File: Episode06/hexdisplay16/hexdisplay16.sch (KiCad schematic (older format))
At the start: 24 parts, among them J1 Conn_02x05_Counter_Clockwise, J2 Conn_02x05_Counter_Clockwise, J3 Conn_02x05_Counter_Clockwise, J4 Conn_02x05_Counter_Clockwise, J5 Conn_01x02, J6 Conn_01x16, J7 Conn_01x06, Q1 MMBT3906, Q2 MMBT3906, Q3 MMBT3906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

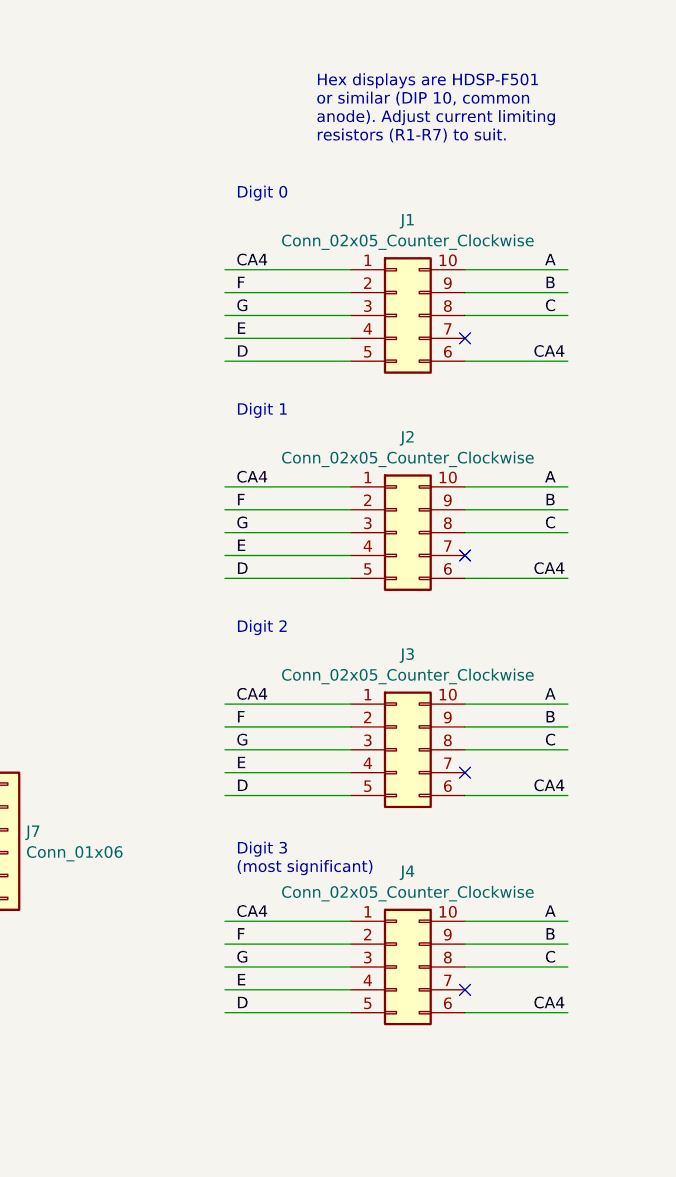
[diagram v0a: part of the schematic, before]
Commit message: fix common anode lines
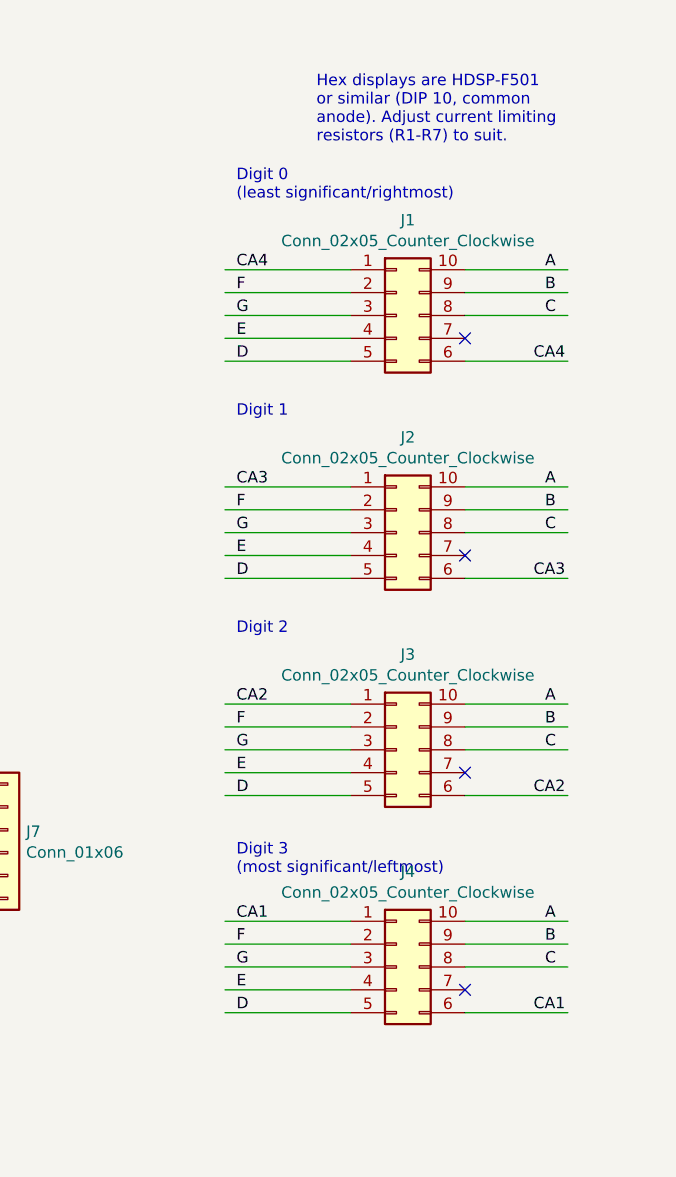
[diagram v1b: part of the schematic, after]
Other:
- note added: "Digit 0\n(least significant/rightmost)"
- note added: "Digit 3\n(most significant/leftmost)"
- note removed: "Digit 0"
- note removed: "Digit 3\n(most significant)"
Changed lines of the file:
@@
 Digit 1
 Text Notes 8500 2750 0    50   ~ 0
-Digit 0
+Digit 0\n(least significant/rightmost)
 Wire Wire Line
 	9000 3050 8450 3050
@@
 $EndComp
 Text Notes 8500 5700 0    50   ~ 0
-Digit 3\n(most significant)
+Digit 3\n(most significant/leftmost)
 Wire Wire Line
 	9000 3350 8450 3350
@@
 	9000 4000 8450 4000
 Text Label 8500 4000 0    50   ~ 0
-CA4
+CA3
 Wire Wire Line
 	9000 4400 8450 4400
@@
 	9000 4950 8450 4950
 Text Label 8500 4950 0    50   ~ 0
-CA4
+CA2
 Wire Wire Line
 	9000 5350 8450 5350
@@
 	9000 5900 8450 5900
 Text Label 8500 5900 0    50   ~ 0
-CA4
+CA1
 Wire Wire Line
 	9000 6300 8450 6300
@@
 	9500 4400 9950 4400
 Text Label 9800 4400 0    50   ~ 0
-CA4
+CA3
 Wire Wire Line
 	9500 4000 9950 4000
@@
 	9500 5350 9950 5350
 Text Label 9800 5350 0    50   ~ 0
-CA4
+CA2
 Wire Wire Line
 	9500 4950 9950 4950
@@
 	9500 6300 9950 6300
 Text Label 9800 6300 0    50   ~ 0
-CA4
+CA1
 Wire Wire Line
 	9500 5900 9950 5900

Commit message: assign packages
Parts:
- C1: footprint (none) -> Capacitor_SMD:C_1206_3216Metric_Pad1.33x1.80mm_HandSolder
- J1, J2, J3, J4: footprint (none) -> Package_DIP:DIP-10_W7.62mm
- J5: footprint (none) -> Connector_PinHeader_2.54mm:PinHeader_1x02_P2.54mm_Vertical
- J6: footprint (none) -> Connector_PinHeader_2.54mm:PinHeader_1x16_P2.54mm_Vertical
- J7: footprint (none) -> Connector_PinHeader_2.54mm:PinHeader_1x06_P2.54mm_Vertical
- Q1, Q2, Q3, Q4: footprint SOT95P240X120-3N -> Package_TO_SOT_SMD:SOT-23
- R1, R10, R11, R2, R3, R4, R5, R6, R7, R8, R9: footprint (none) -> Resistor_SMD:R_0805_2012Metric_Pad1.20x1.40mm_HandSolder
- U1: footprint QFP80P1200X1200X120-44N -> Package_QFP:LQFP-44_10x10mm_P0.8mm
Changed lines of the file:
@@
 F 0 "U1" H 4450 4170 50  0000 C CNN
 F 1 "ATMEGA164A-AU" H 4450 4079 50  0000 C CNN
-F 2 "QFP80P1200X1200X120-44N" H 4450 2400 50  0001 L BNN
+F 2 "Package_QFP:LQFP-44_10x10mm_P0.8mm" H 4450 2400 50  0001 L BNN
 F 3 "" H 4450 2400 50  0001 L BNN
 F 4 "1841601" H 4450 2400 50  0001 L BNN "OC_FARNELL"
@@
 F 0 "R1" V 1100 1650 50  0000 C CNN
 F 1 "330" V 1150 1900 50  0000 C CNN
-F 2 "" V 1080 1900 50  0001 C CNN
+F 2 "Resistor_SMD:R_0805_2012Metric_Pad1.20x1.40mm_HandSolder" V 1080 1900 50  0001 C CNN
 F 3 "" H 1150 1900 50  0001 C CNN
 	1    1150 1900
@@
 F 0 "R2" V 1100 1750 50  0000 C CNN
 F 1 "330" V 1150 2000 50  0000 C CNN
-F 2 "" V 1080 2000 50  0001 C CNN
+F 2 "Resistor_SMD:R_0805_2012Metric_Pad1.20x1.40mm_HandSolder" V 1080 2000 50  0001 C CNN
 F 3 "" H 1150 2000 50  0001 C CNN
 	1    1150 2000
@@
 F 0 "R3" V 1100 1850 50  0000 C CNN
 F 1 "330" V 1150 2100 50  0000 C CNN
-F 2 "" V 1080 2100 50  0001 C CNN
+F 2 "Resistor_SMD:R_0805_2012Metric_Pad1.20x1.40mm_HandSolder" V 1080 2100 50  0001 C CNN
 F 3 "" H 1150 2100 50  0001 C CNN
 	1    1150 2100
@@
 F 0 "R4" V 1100 1950 50  0000 C CNN
 F 1 "330" V 1150 2200 50  0000 C CNN
-F 2 "" V 1080 2200 50  0001 C CNN
+F 2 "Resistor_SMD:R_0805_2012Metric_Pad1.20x1.40mm_HandSolder" V 1080 2200 50  0001 C CNN
 F 3 "" H 1150 2200 50  0001 C CNN
 	1    1150 2200
@@
 F 0 "R5" V 1100 2050 50  0000 C CNN
 F 1 "330" V 1150 2300 50  0000 C CNN
-F 2 "" V 1080 2300 50  0001 C CNN
+F 2 "Resistor_SMD:R_0805_2012Metric_Pad1.20x1.40mm_HandSolder" V 1080 2300 50  0001 C CNN
 F 3 "" H 1150 2300 50  0001 C CNN
 	1    1150 2300
@@
 F 0 "R6" V 1100 2150 50  0000 C CNN
 F 1 "330" V 1150 2400 50  0000 C CNN
-F 2 "" V 1080 2400 50  0001 C CNN
+F 2 "Resistor_SMD:R_0805_2012Metric_Pad1.20x1.40mm_HandSolder" V 1080 2400 50  0001 C CNN
 F 3 "" H 1150 2400 50  0001 C CNN
 	1    1150 2400
@@
 F 0 "R7" V 1100 2250 50  0000 C CNN
 F 1 "330" V 1150 2500 50  0000 C CNN
-F 2 "" V 1080 2500 50  0001 C CNN
+F 2 "Resistor_SMD:R_0805_2012Metric_Pad1.20x1.40mm_HandSolder" V 1080 2500 50  0001 C CNN
 F 3 "" H 1150 2500 50  0001 C CNN
 	1    1150 2500
@@
 F 0 "Q1" H 2453 5046 50  0000 L CNN
 F 1 "MMBT3906" H 2453 4955 50  0000 L CNN
-F 2 "SOT95P240X120-3N" H 2300 5000 50  0001 L BNN
+F 2 "Package_TO_SOT_SMD:SOT-23" H 2300 5000 50  0001 L BNN
 F 3 "" H 2300 5000 50  0001 L BNN
 F 4 "Fairchild Semiconductor" H 2300 5000 50  0001 L BNN "MANUFACTURER"
@@
 F 0 "R8" V 1593 5000 50  0000 C CNN
 F 1 "4k7" V 1684 5000 50  0000 C CNN
-F 2 "" V 1730 5000 50  0001 C CNN
+F 2 "Resistor_SMD:R_0805_2012Metric_Pad1.20x1.40mm_HandSolder" V 1730 5000 50  0001 C CNN
 F 3 "" H 1800 5000 50  0001 C CNN
 	1    1800 5000
@@
 F 0 "Q2" H 2553 5846 50  0000 L CNN
 F 1 "MMBT3906" H 2553 5755 50  0000 L CNN
-F 2 "SOT95P240X120-3N" H 2400 5800 50  0001 L BNN
+F 2 "Package_TO_SOT_SMD:SOT-23" H 2400 5800 50  0001 L BNN
 F 3 "" H 2400 5800 50  0001 L BNN
 F 4 "Fairchild Semiconductor" H 2400 5800 50  0001 L BNN "MANUFACTURER"
@@
 F 0 "R9" V 1693 5800 50  0000 C CNN
 F 1 "4k7" V 1784 5800 50  0000 C CNN
-F 2 "" V 1830 5800 50  0001 C CNN
+F 2 "Resistor_SMD:R_0805_2012Metric_Pad1.20x1.40mm_HandSolder" V 1830 5800 50  0001 C CNN
 F 3 "" H 1900 5800 50  0001 C CNN
 	1    1900 5800
@@
 F 0 "Q3" H 2653 6646 50  0000 L CNN
 F 1 "MMBT3906" H 2653 6555 50  0000 L CNN
-F 2 "SOT95P240X120-3N" H 2500 6600 50  0001 L BNN
+F 2 "Package_TO_SOT_SMD:SOT-23" H 2500 6600 50  0001 L BNN
 F 3 "" H 2500 6600 50  0001 L BNN
 F 4 "Fairchild Semiconductor" H 2500 6600 50  0001 L BNN "MANUFACTURER"
@@
 F 0 "R10" V 1793 6600 50  0000 C CNN
 F 1 "4k7" V 1884 6600 50  0000 C CNN
-F 2 "" V 1930 6600 50  0001 C CNN
+F 2 "Resistor_SMD:R_0805_2012Metric_Pad1.20x1.40mm_HandSolder" V 1930 6600 50  0001 C CNN
 F 3 "" H 2000 6600 50  0001 C CNN
 	1    2000 6600
@@
 F 0 "Q4" H 2753 7446 50  0000 L CNN
 F 1 "MMBT3906" H 2753 7355 50  0000 L CNN
-F 2 "SOT95P240X120-3N" H 2600 7400 50  0001 L BNN
+F 2 "Package_TO_SOT_SMD:SOT-23" H 2600 7400 50  0001 L BNN
 F 3 "" H 2600 7400 50  0001 L BNN
 F 4 "Fairchild Semiconductor" H 2600 7400 50  0001 L BNN "MANUFACTURER"
@@
 F 0 "R11" V 1893 7400 50  0000 C CNN
 F 1 "4k7" V 1984 7400 50  0000 C CNN
-F 2 "" V 2030 7400 50  0001 C CNN
+F 2 "Resistor_SMD:R_0805_2012Metric_Pad1.20x1.40mm_HandSolder" V 2030 7400 50  0001 C CNN
 F 3 "" H 2100 7400 50  0001 C CNN
 	1    2100 7400
@@
 	5400 5250 5400 5400
 $Comp
-L power:VCC #PWR?
+L power:VCC #PWR0101
 U 1 1 606C797B
 P 5400 4900
-F 0 "#PWR?" H 5400 4750 50  0001 C CNN
+F 0 "#PWR0101" H 5400 4750 50  0001 C CNN
 F 1 "VCC" H 5417 5073 50  0000 C CNN
 F 2 "" H 5400 4900 50  0001 C CNN
@@
 $EndComp
 $Comp
-L power:GND #PWR?
+L power:GND #PWR0102
 U 1 1 606C80BF
 P 5400 5500
-F 0 "#PWR?" H 5400 5250 50  0001 C CNN
+F 0 "#PWR0102" H 5400 5250 50  0001 C CNN
 F 1 "GND" H 5405 5327 50  0000 C CNN
 F 2 "" H 5400 5500 50  0001 C CNN
@@
 F 0 "C1" H 5815 5246 50  0000 L CNN
 F 1 "100nF" H 5815 5155 50  0000 L CNN
-F 2 "" H 5738 5050 50  0001 C CNN
+F 2 "Capacitor_SMD:C_1206_3216Metric_Pad1.33x1.80mm_HandSolder" H 5738 5050 50  0001 C CNN
 F 3 "" H 5700 5200 50  0001 C CNN
 	1    5700 5200
@@
 F 0 "J5" H 4768 4925 50  0000 C CNN
 F 1 "Conn_01x02" H 4768 5016 50  0000 C CNN
-F 2 "" H 4850 5250 50  0001 C CNN
+F 2 "Connector_PinHeader_2.54mm:PinHeader_1x02_P2.54mm_Vertical" H 4850 5250 50  0001 C CNN
 F 3 "~" H 4850 5250 50  0001 C CNN
 	1    4850 5250
@@
 F 0 "J6" H 5680 6892 50  0000 L CNN
 F 1 "Conn_01x16" H 5680 6801 50  0000 L CNN
-F 2 "" H 5600 6900 50  0001 C CNN
+F 2 "Connector_PinHeader_2.54mm:PinHeader_1x16_P2.54mm_Vertical" H 5600 6900 50  0001 C CNN
 F 3 "~" H 5600 6900 50  0001 C CNN
 	1    5600 6900
@@
 F 0 "J7" H 7580 5492 50  0000 L CNN
 F 1 "Conn_01x06" H 7580 5401 50  0000 L CNN
-F 2 "" H 7500 5500 50  0001 C CNN
+F 2 "Connector_PinHeader_2.54mm:PinHeader_1x06_P2.54mm_Vertical" H 7500 5500 50  0001 C CNN
 F 3 "~" H 7500 5500 50  0001 C CNN
 	1    7500 5500
@@
 F 0 "J1" H 9250 3667 50  0000 C CNN
 F 1 "Conn_02x05_Counter_Clockwise" H 9250 3576 50  0000 C CNN
-F 2 "" H 9200 3250 50  0001 C CNN
+F 2 "Package_DIP:DIP-10_W7.62mm" H 9200 3250 50  0001 C CNN
 F 3 "~" H 9200 3250 50  0001 C CNN
 	1    9200 3250
@@
 F 0 "J2" H 9250 4617 50  0000 C CNN
 F 1 "Conn_02x05_Counter_Clockwise" H 9250 4526 50  0000 C CNN
-F 2 "" H 9200 4200 50  0001 C CNN
+F 2 "Package_DIP:DIP-10_W7.62mm" H 9200 4200 50  0001 C CNN
 F 3 "~" H 9200 4200 50  0001 C CNN
 	1    9200 4200
@@
 F 0 "J3" H 9250 5567 50  0000 C CNN
 F 1 "Conn_02x05_Counter_Clockwise" H 9250 5476 50  0000 C CNN
-F 2 "" H 9200 5150 50  0001 C CNN
+F 2 "Package_DIP:DIP-10_W7.62mm" H 9200 5150 50  0001 C CNN
 F 3 "~" H 9200 5150 50  0001 C CNN
 	1    9200 5150
@@
 F 0 "J4" H 9250 6517 50  0000 C CNN
 F 1 "Conn_02x05_Counter_Clockwise" H 9250 6426 50  0000 C CNN
-F 2 "" H 9200 6100 50  0001 C CNN
+F 2 "Package_DIP:DIP-10_W7.62mm" H 9200 6100 50  0001 C CNN
 F 3 "~" H 9200 6100 50  0001 C CNN
 	1    9200 6100

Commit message: minor schematic updates, regenerated PDFs
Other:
- note added: "atmega324, 644, and 1284 variants in\nTQFP-44 packages should also work"
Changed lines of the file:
@@
 NoConn ~ 9500 5250
 NoConn ~ 9500 6200
+Text Notes 4950 700  0    50   ~ 0
+atmega324, 644, and 1284 variants in\nTQFP-44 packages should also work
 $EndSCHEMATC
